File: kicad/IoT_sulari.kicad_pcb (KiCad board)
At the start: 4 copper layers, 48 parts, among them J1 73412-0110, J2 73412-0110, J20 694106106102, J3 20021121-00010C4LF, J4 20021121-00010C4LF, J40 693043020611, J5 20021121-00010C4LF, J6 20021121-00010C4LF, SW1 SW_SPST, SW2 TL3301DF160QG, SW3 TL3301DF160QG, SW4 TL3301DF160QG, SW5 TL3301DF160QG, U2 NRF9160, U20 MIC5219-3.3YM5-TR, U30 SHT40-AD1B-R2, U31 TMP117MAIDRVT, U40 TPD3F303DPVR

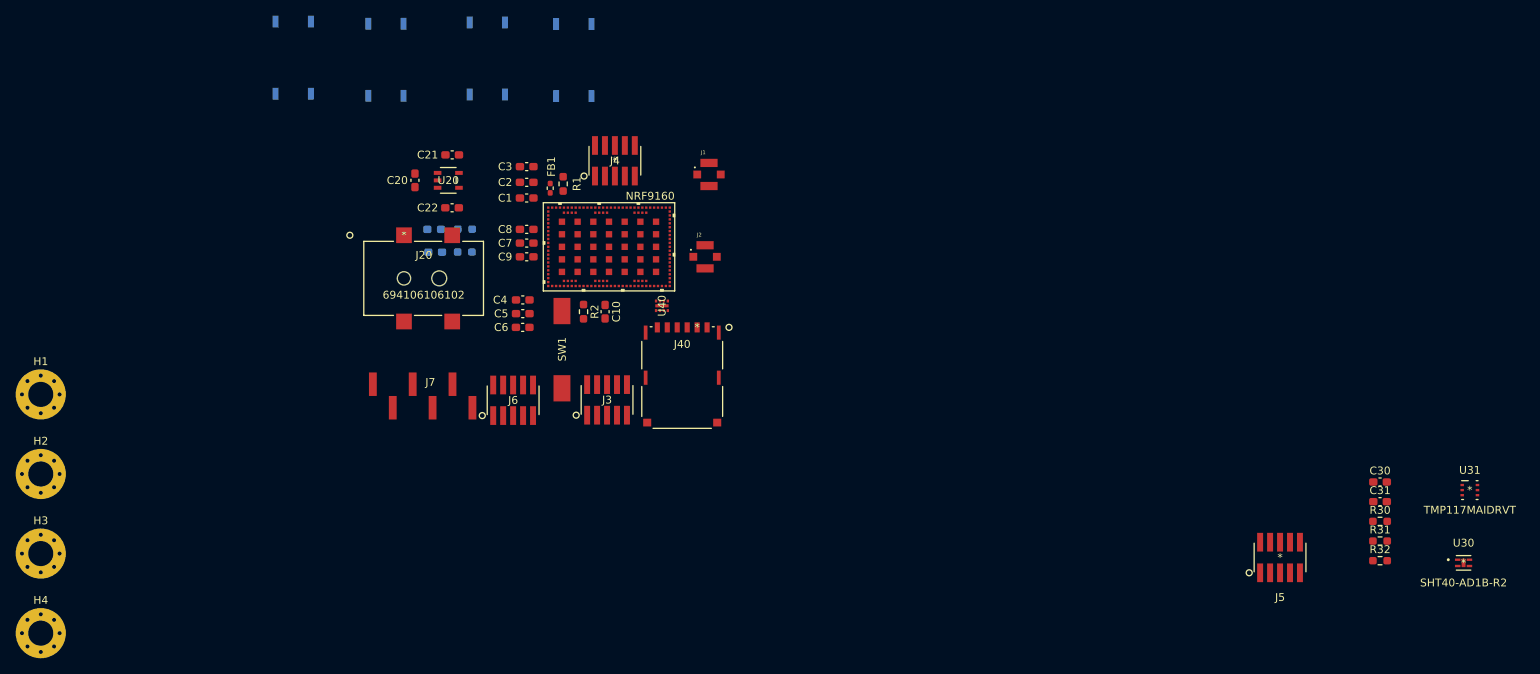
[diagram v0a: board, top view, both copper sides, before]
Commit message: added board outline and inner copper layers, layout finalization
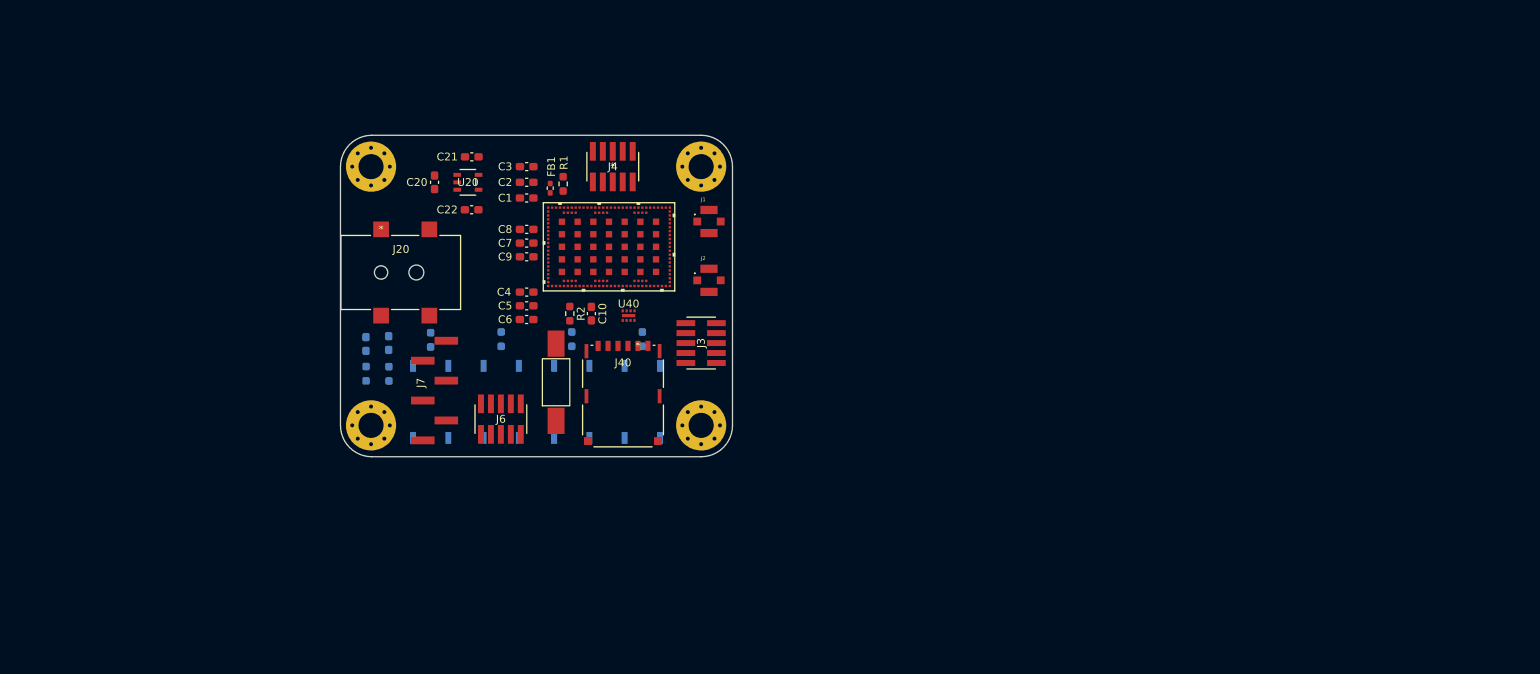
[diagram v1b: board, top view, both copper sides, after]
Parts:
- removed C30, C31: 100n, Capacitor_SMD:C_0603_1608Metric_Pad1.08x0.95mm_HandSolder
- removed J5: 20021121-00010C4LF, 20021121-00010C4LF:20021121-00010C4LF
- removed R30, R31, R32: 5k, Resistor_SMD:R_0603_1608Metric_Pad0.98x0.95mm_HandSolder
- removed U30: SHT40-AD1B-R2, SHT-40AD1B-R2:SHT40-AD1B-R2
- removed U31: TMP117MAIDRVT, TMP117MAIDRVT:TMP117MAIDRVT
- added R5: 10k, Resistor_SMD:R_0603_1608Metric_Pad0.98x0.95mm_HandSolder, B.Cu at (131.0, 61.0)
- added R6: 10k, Resistor_SMD:R_0603_1608Metric_Pad0.98x0.95mm_HandSolder, B.Cu at (122.0, 61.0)
- added R7: 10k, Resistor_SMD:R_0603_1608Metric_Pad0.98x0.95mm_HandSolder, B.Cu at (113.0, 61.0)
- added R8: 10k, Resistor_SMD:R_0603_1608Metric_Pad0.98x0.95mm_HandSolder, B.Cu at (104.0, 61.1)
- moved H2 92.9 mm to (138.5, 39.0)
- moved H3 85.8 mm to (138.5, 72.0)
- moved H1 51.2 mm to (96.4, 39.0)
- moved H4 49.8 mm to (96.4, 72.0)
- moved SW5 47.3 mm to (104.0, 69.0)
- moved SW4 46.0 mm to (113.0, 69.0)
- moved SW3 45.1 mm to (122.0, 69.0)
- moved SW2 44.5 mm to (131.0, 69.0)
- moved R3 20.8 mm to (98.7, 65.4), turned to -90 degrees
- moved R4 20.0 mm to (95.8, 65.4), turned to -90 degrees
- moved D1 15.6 mm to (98.7, 61.5), turned to 90 degrees
- moved D2 14.7 mm to (95.8, 61.6), turned to 90 degrees
- moved J3 14.0 mm to (138.5, 61.5), turned to 90 degrees
- moved J40 7.91 mm to (130.4, 61.9)
- moved J1 6.00 mm to (139.5, 46.0)
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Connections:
- SW2 pad 3: GND -> Net-(R5-Pad2)
- SW2 pad 4: GND -> Net-(R5-Pad2)
- SW3 pad 3: GND -> Net-(R6-Pad2)
- SW3 pad 4: GND -> Net-(R6-Pad2)
- SW4 pad 3: GND -> Net-(R7-Pad2)
- SW4 pad 4: GND -> Net-(R7-Pad2)
- SW5 pad 3: GND -> Net-(R8-Pad2)
- SW5 pad 4: GND -> Net-(R8-Pad2)
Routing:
- added copper zone on In2.Cu, net +3.3V
- added copper zone on In1.Cu, net GND
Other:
- board outline added: 50 x 41 mm

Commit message: routing
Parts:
- C10, R2: moved to B.Cu
- moved D2 44.7 mm to (140.2, 66.3), turned to -90 degrees
- moved R4 44.5 mm to (140.2, 62.5), turned to 90 degrees
- moved D1 39.0 mm to (137.3, 66.4), turned to -90 degrees
- moved R3 38.7 mm to (137.3, 62.5), turned to 90 degrees
- moved SW1 20.4 mm to (99.9, 63.1), turned to 0 degrees
- moved C10 15.9 mm to (108.6, 56.9), turned to 180 degrees
- moved R2 12.4 mm to (109.5, 59.4)
- moved J6 6.01 mm to (119.0, 71.2)
- moved J7 4.77 mm to (107.3, 71.4), turned to 180 degrees
- moved J4 2.37 mm to (129.6, 39.1)
- moved U40 2.24 mm to (131.4, 57.2)
- moved C20 1.00 mm to (103.5, 41.0)
- moved R1 0.85 mm to (121.2, 40.4)
- moved C8 0.75 mm to (116.2, 47.8)
- moved J40 0.63 mm to (131.1, 61.9)
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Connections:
- net /+3.3V renamed Net-(C1-Pad1)
- U2 pad 25: CS -> DC
- U2 pad 26: DC -> BUSY
- U2 pad 28: RST -> CS
- U2 pad 29: BUSY -> RST
- U2 pad 83: SDA -> TMP_ALERT
- U2 pad 84: SCL -> SDA
- U2 pad 86: TMP_ALERT -> SCL
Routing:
- net NRESET: track 0.00 -> 33.7 mm, vias 0 -> 2
- net UART_RTS: track 0.00 -> 30.6 mm
- net UART_RXD: track 0.00 -> 30.2 mm
- net UART_TXD: track 0.00 -> 25.2 mm
- net DIN: track 0.00 -> 23.0 mm
- net UART_CTS: track 0.00 -> 22.3 mm
- net CS: track 0.00 -> 21.9 mm
- net RST: track 0.00 -> 21.0 mm
- net Net-(U20-EN): track 0.00 -> 19.7 mm
- net CLK: track 0.00 -> 16.1 mm
- net DC: track 0.00 -> 15.8 mm
- net BUSY: track 0.00 -> 15.5 mm
- net Net-(U40-DATA1_OUT): track 0.00 -> 13.0 mm
- net SIM_1V8: track 0.00 -> 10.3 mm
- net SCL: track 0.00 -> 9.26 mm
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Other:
- board size 50 x 41 mm -> 50.5 x 41 mm

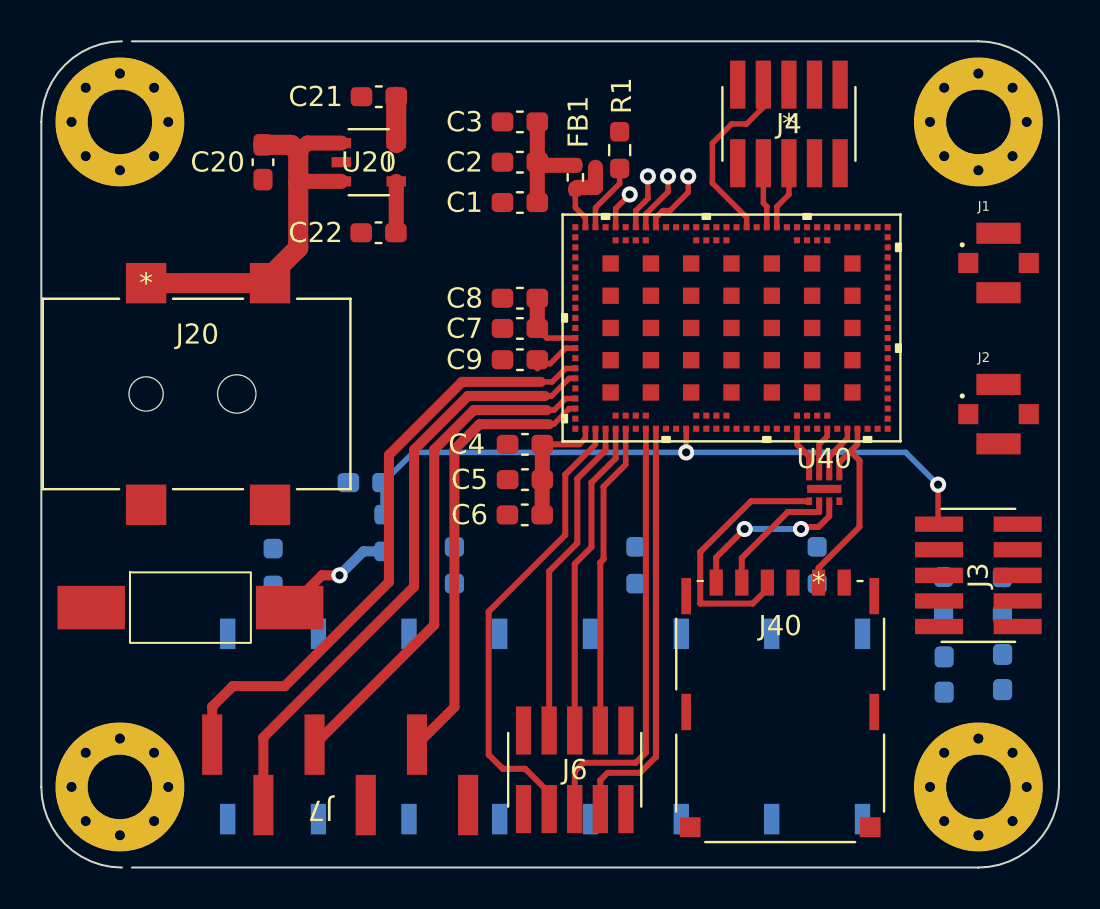
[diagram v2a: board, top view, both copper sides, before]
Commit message: Finished routing and added vias
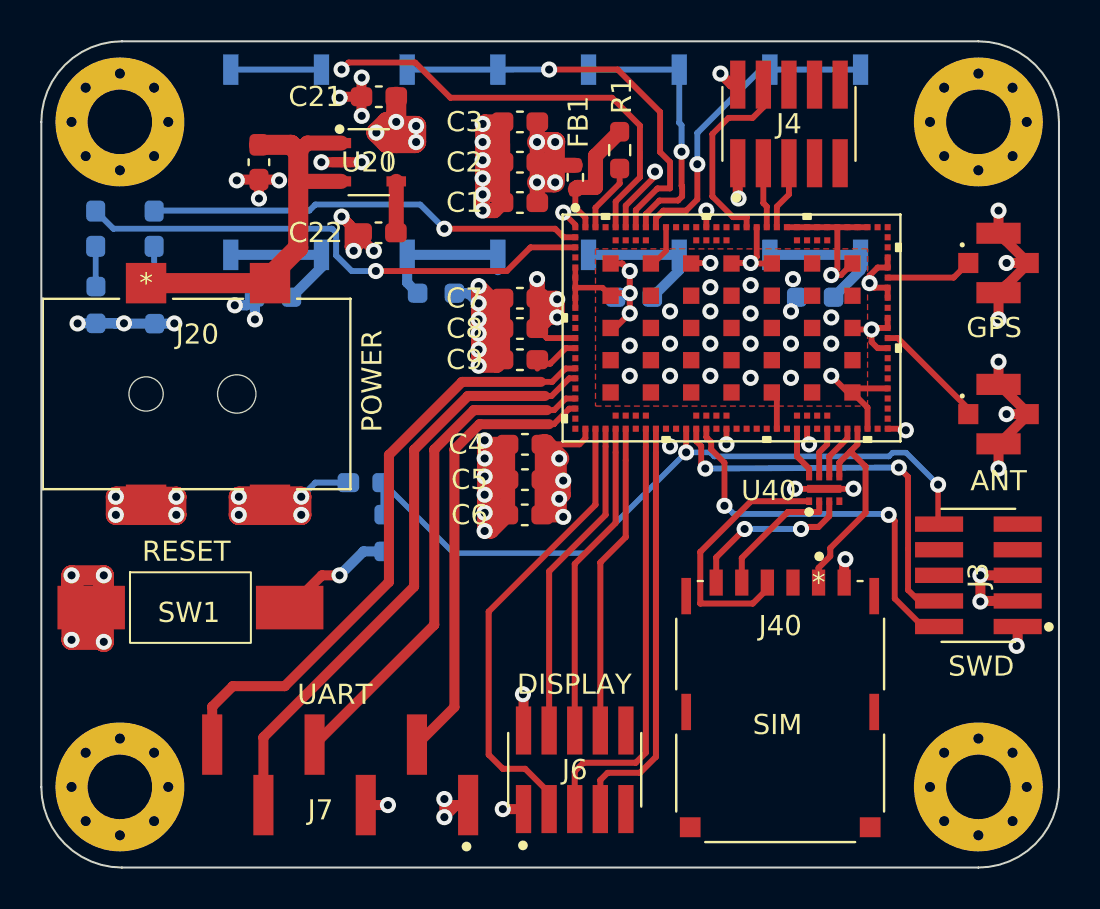
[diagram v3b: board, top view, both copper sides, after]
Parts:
- moved D2 50.1 mm to (95.2, 44.3), turned to 90 degrees
- moved R4 47.2 mm to (95.2, 48.1), turned to -90 degrees
- moved D1 45.0 mm to (98.1, 44.3), turned to 90 degrees
- moved R3 41.7 mm to (98.1, 48.1), turned to -90 degrees
- moved SW5 28.0 mm to (104.2, 41.0), turned to -90 degrees
- moved SW2 28.0 mm to (130.9, 41.0), turned to -90 degrees
- moved SW3 28.0 mm to (121.9, 41.0), turned to -90 degrees
- moved SW4 28.0 mm to (112.9, 41.0), turned to -90 degrees
- moved R7 13.5 mm to (112.1, 47.5), turned to 180 degrees
- moved R8 13.4 mm to (104.0, 47.7), turned to 0 degrees
- moved R5 13.3 mm to (130.9, 47.7), turned to 0 degrees
- moved R6 13.3 mm to (121.9, 47.7), turned to 0 degrees
- moved C20 0.20 mm to (103.3, 41.0)
- renumbered C8 to C7, C7 to C8
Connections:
- C1 pad 1: Net-(C1-Pad1) -> +3.3V
- C2 pad 1: Net-(C1-Pad1) -> +3.3V
- C3 pad 1: Net-(C1-Pad1) -> +3.3V
- C4 pad 1: /VDD2 -> +3.3V
- C5 pad 1: /VDD2 -> +3.3V
- C6 pad 1: /VDD2 -> +3.3V
- C7 pad 1: /VDD_GPIO -> +3.3V
- C8 pad 1: /VDD_GPIO -> +3.3V
- FB1 pad 2: Net-(C1-Pad1) -> +3.3V
- J3 pad 1: Net-(J3-Pad1) -> +3.3V
- J4 pad 1: /SENSORBOARD_PWR -> +3.3V
- J6 pad 1: /DISPLAY_PWR -> +3.3V
- J7 pad 3: UART_VCC -> +3.3V
- U2 pad 1: /GND_SHIELD-GND -> GND
- U2 pad 11: /GND_SHIELD-GND -> GND
- U2 pad 12: /VDD_GPIO -> +3.3V
- U2 pad 14: /GND_SHIELD-GND -> GND
- U2 pad 17: /GND_SHIELD-GND -> GND
- U2 pad 21: /GND_SHIELD-GND -> GND
- U2 pad 22: /VDD2 -> +3.3V
- U2 pad 27: /GND_SHIELD-GND -> GND
- U2 pad 31: /GND_SHIELD-GND -> GND
- U2 pad 36: /GND_SHIELD-GND -> GND
- U2 pad 41: /GND_SHIELD-GND -> GND
- U2 pad 44: /GND_SHIELD-GND -> GND
- U2 pad 47: /GND_SHIELD-GND -> GND
- U2 pad 5: /GND_SHIELD-GND -> GND
- U2 pad 50: /GND_SHIELD-GND -> GND
- U2 pad 52: /GND_SHIELD-GND -> GND
- U2 pad 56: /GND_SHIELD-GND -> GND
- U2 pad 6: /GND_SHIELD-GND -> GND
- U2 pad 60: /GND_SHIELD-GND -> GND
- U2 pad 62: /GND_SHIELD-GND -> GND
- U2 pad 63: /GND_SHIELD-GND -> GND
- U2 pad 65: /GND_SHIELD-GND -> GND
- U2 pad 66: /GND_SHIELD-GND -> GND
- U2 pad 68: /GND_SHIELD-GND -> GND
- U2 pad 69: /GND_SHIELD-GND -> GND
- U2 pad 7: /GND_SHIELD-GND -> GND
- U2 pad 72: /GND_SHIELD-GND -> GND
- U2 pad 74: /GND_SHIELD-GND -> GND
- U2 pad 75: /GND_SHIELD-GND -> GND
- U2 pad 76: /GND_SHIELD-GND -> GND
- U2 pad 77: /GND_SHIELD-GND -> GND
- U2 pad 78: /GND_SHIELD-GND -> GND
- U2 pad 79: /GND_SHIELD-GND -> GND
- U2 pad 8: /GND_SHIELD-GND -> GND
- U2 pad 80: /GND_SHIELD-GND -> GND
- U2 pad 81: /GND_SHIELD-GND -> GND
- U2 pad 82: /GND_SHIELD-GND -> GND
- U2 pad 85: /GND_SHIELD-GND -> GND
- U2 pad 9: /GND_SHIELD-GND -> GND
- U2 pad 90: /GND_SHIELD-GND -> GND
- U2 pad 94: /GND_SHIELD-GND -> GND
- U2 pad 98: /GND_SHIELD-GND -> GND
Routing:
- net GND: track 0.00 -> 216.2 mm, vias 0 -> 96
- net +3.3V: track 2.30 -> 47.4 mm, vias 0 -> 19
- net STATUS_LED_GREEN: track 0.00 -> 26.2 mm, vias 0 -> 1
- net BUTTON4: track 1.91 -> 26.5 mm
- net STATUS_LED_RED: track 0.00 -> 21.7 mm, vias 0 -> 1
- net SWDCLK: track 0.00 -> 20.7 mm, vias 0 -> 2
- net SWDIO: track 0.00 -> 19.7 mm, vias 0 -> 2
- net BUTTON3: track 2.77 -> 20.4 mm
- net BUTTON1: track 3.40 -> 15.6 mm
- net BUTTON2: track 2.98 -> 13.7 mm
- net Net-(R7-Pad2): track 0.00 -> 7.38 mm
- net Net-(R8-Pad2): track 0.00 -> 7.22 mm
- net Net-(R5-Pad2): track 0.00 -> 7.16 mm
- net Net-(R6-Pad2): track 0.00 -> 7.16 mm
- net /VDD2: track 6.23 -> 0.00 mm
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- added copper zone on F.Cu, net GND
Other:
- outline, holes or cut-outs redrawn
- board text added: "ANT"
- board text added: "BUTTON1"
- board text added: "BUTTON2"
- board text added: "BUTTON3"
- board text added: "BUTTON4"
- board text added: "DISPLAY"
- board text added: "GPS"
- board text added: "POWER"
- board text added: "RESET"
- board text added: "SIM"
- board text added: "SWD"
- board text added: "UART"

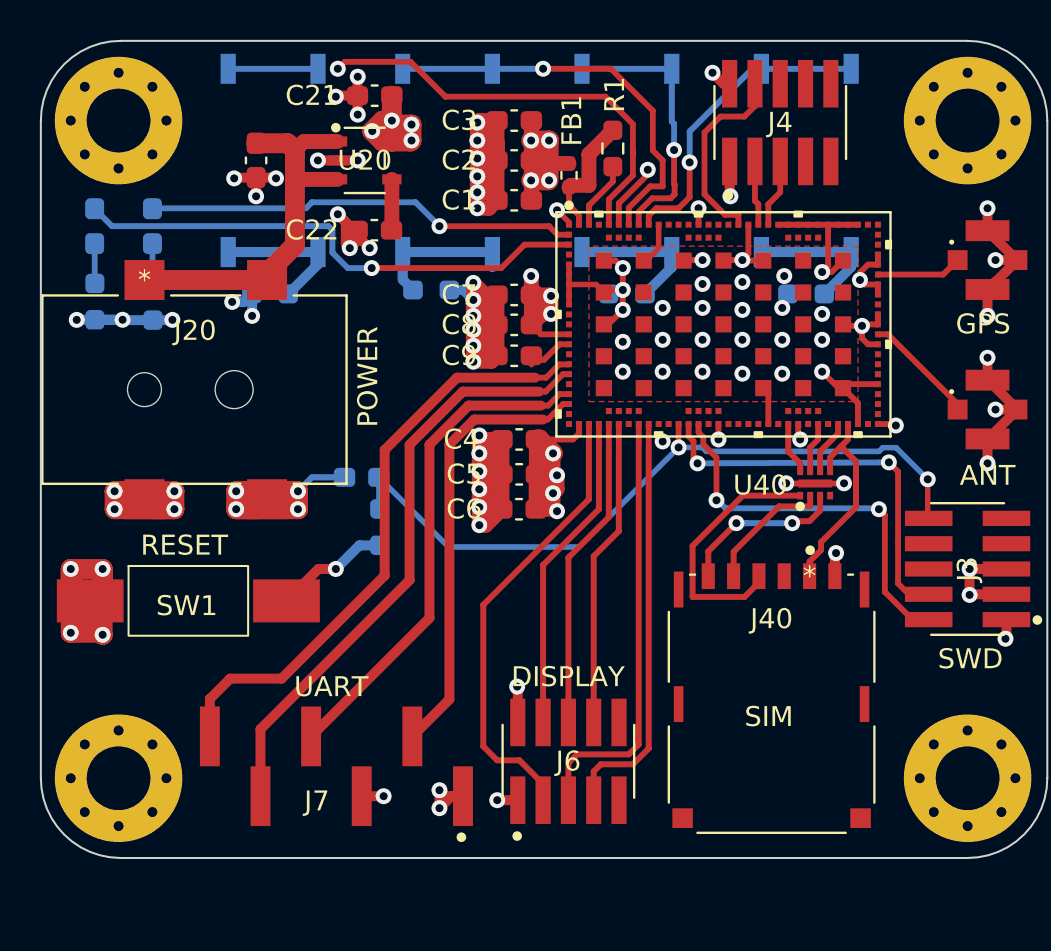
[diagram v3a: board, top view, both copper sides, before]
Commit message: Fixed drc errors for PCB
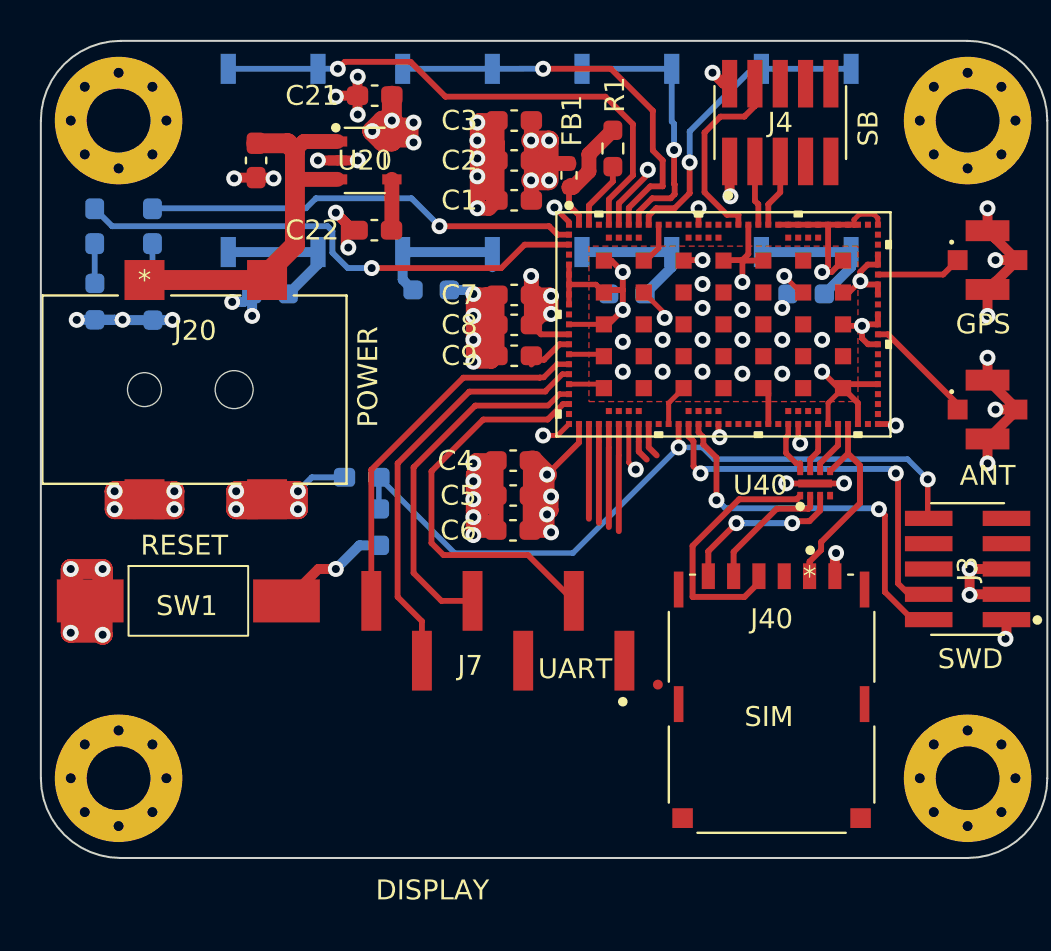
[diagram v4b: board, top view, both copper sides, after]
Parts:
- removed J6: 20021121-00010C4LF, 20021121-00010C4LF:20021121-00010C4LF
- moved J7 10.6 mm to (115.4, 64.6)
- moved C4 1.10 mm to (116.2, 56.1)
- moved C5 1.10 mm to (116.2, 57.8)
- moved C6 1.10 mm to (116.2, 59.6)
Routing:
- net CS: track 21.9 -> 1.95 mm
- net RST: track 21.0 -> 1.74 mm
- net DIN: track 23.0 -> 4.75 mm
- net UART_RTS: track 30.6 -> 18.7 mm
- net CLK: track 16.1 -> 4.96 mm
- net DC: track 15.8 -> 5.17 mm
- net BUSY: track 15.5 -> 5.38 mm
- net UART_RXD: track 30.2 -> 20.9 mm
- net GND: track 216.2 -> 223.5 mm, vias 96 -> 85
- net UART_TXD: track 25.2 -> 18.2 mm
- net UART_CTS: track 22.3 -> 20.2 mm
- net +3.3V: track 47.4 -> 49.4 mm, vias 19 -> 17
- net BUTTON4: track 26.5 -> 27.3 mm
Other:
- board text added: "SB"
